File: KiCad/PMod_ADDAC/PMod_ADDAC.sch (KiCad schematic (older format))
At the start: 22 parts, among them J1 Conn_01x12_Male, J2 AudioJack2_SwitchT, U1 TSX632

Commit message: R2R updated
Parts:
- removed C1: 1u, Capacitor_SMD:C_0805_2012Metric_Pad1.15x1.40mm_HandSolder, symbol Device:C_Small
- added C2: 100, Capacitor_SMD:C_0805_2012Metric_Pad1.15x1.40mm_HandSolder, symbol Device:C_Small
- added R18, R19: 1k, Resistor_SMD:R_0805_2012Metric_Pad1.15x1.40mm_HandSolder, symbol Device:R
- R17: value 8k -> 2k
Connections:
- net GND: now also R17.1, U1.5 (+), C2.2
- net VCC: now also C2.1
- net at R1.2, R9.1: now also R19.2
- net at R17.2: now also JP1.1 (A), U1.3 (+), R19.1
- net at JP1.2 (B), U1.1: now also U1.2 (-), R18.1; no longer J2.T, U1.3 (+)
- net at U1.6 (-): now also U1.7
- new net: J2.T, R18.2
- no-connect marks 4 -> 1
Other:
- moved on the sheet: J1, J2, JP1, R1, R10, R11, R12, R13, R14, R15, R16, R2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

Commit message: r2r
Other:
- note added: "3R?\n"
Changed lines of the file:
@@
 Wire Wire Line
 	4550 2100 4550 2150
+Text Notes 5150 3050 0    50   ~ 0
+3R?\n
 $EndSCHEMATC

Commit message: R2RDAC update
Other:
- note added: "add 6.8n tantalum cap?\nboth VCC and VEE"
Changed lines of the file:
@@
 Text Notes 5150 3050 0    50   ~ 0
 3R?\n
+Text Notes 5950 1550 0    50   ~ 0
+add 6.8n tantalum cap?\nboth VCC and VEE
 $EndSCHEMATC

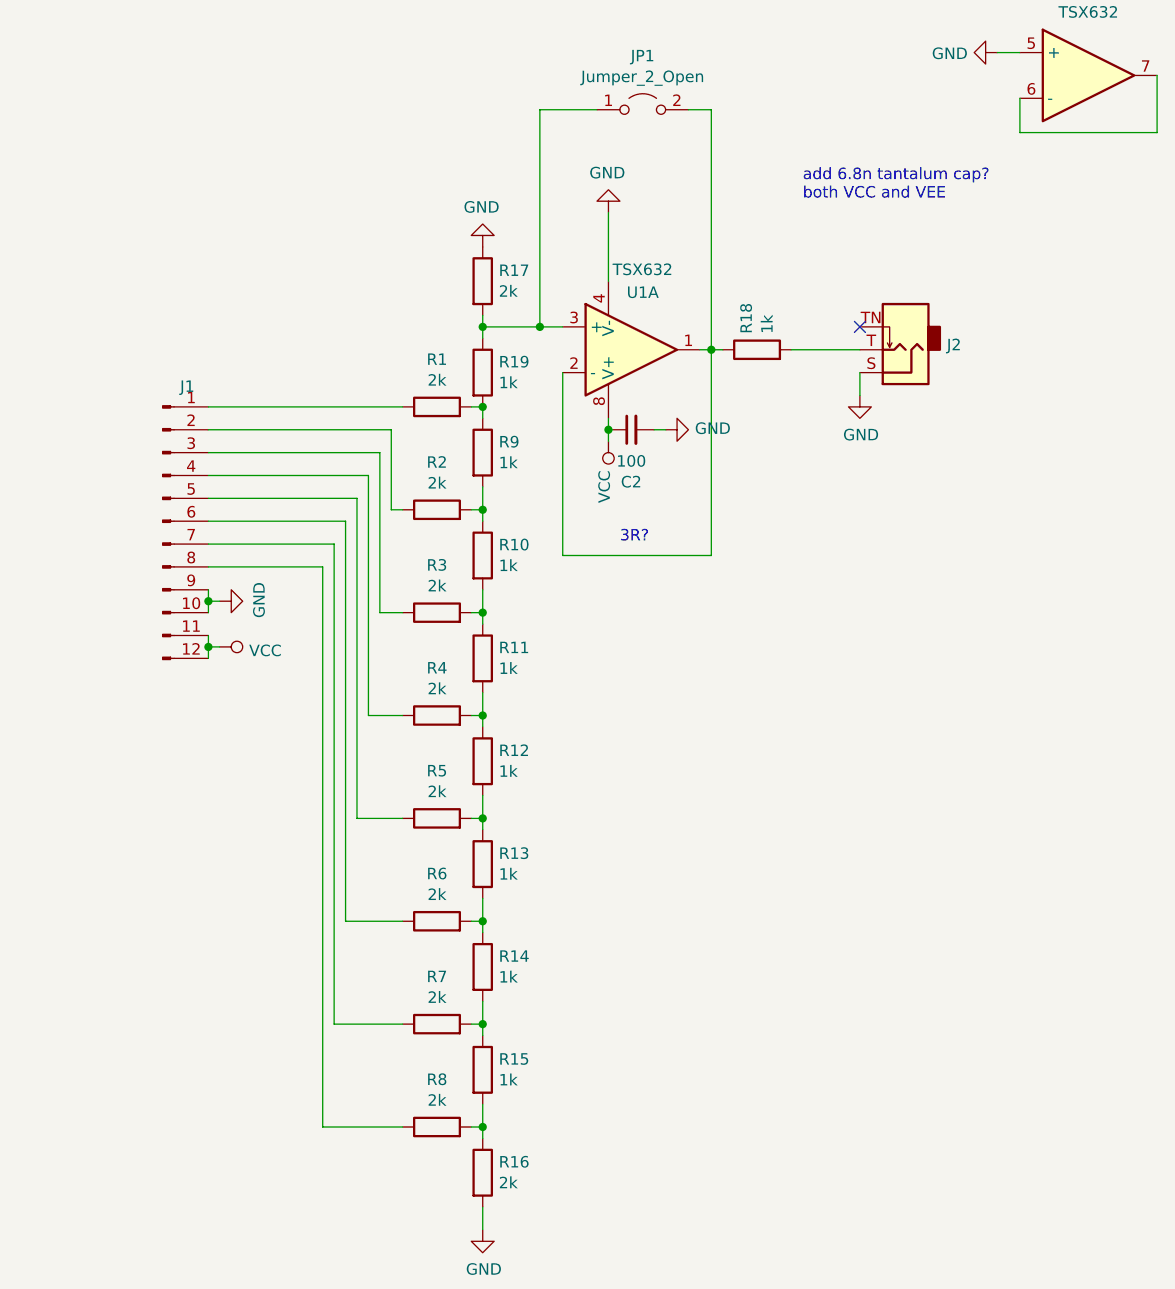
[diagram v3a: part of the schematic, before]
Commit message: fixed R2R orientation
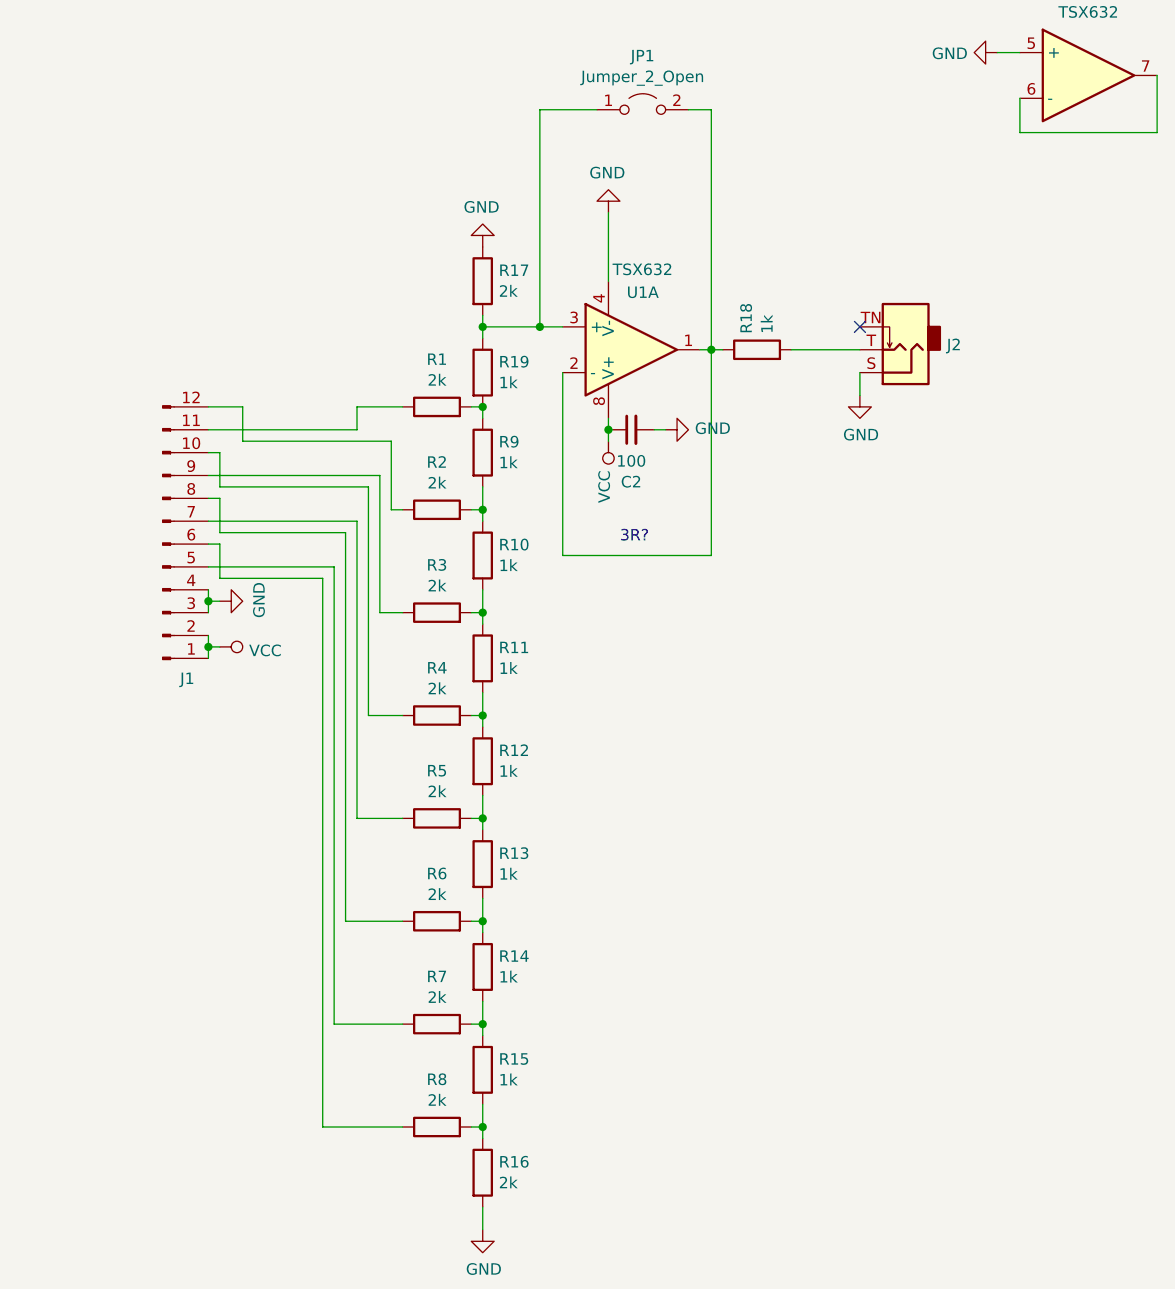
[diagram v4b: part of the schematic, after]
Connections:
- net GND: now also J1.3 (Pin_3), J1.4 (Pin_4); no longer J1.10 (Pin_10), J1.9 (Pin_9)
- net VCC: now also J1.1 (Pin_1), J1.2 (Pin_2); no longer J1.11 (Pin_11), J1.12 (Pin_12)
- net at R1.1: now also J1.11 (Pin_11); no longer J1.1 (Pin_1)
- net at R2.1: now also J1.12 (Pin_12); no longer J1.2 (Pin_2)
- net at R3.1: now also J1.9 (Pin_9); no longer J1.3 (Pin_3)
- net at R4.1: now also J1.10 (Pin_10); no longer J1.4 (Pin_4)
- net at R5.1: now also J1.7 (Pin_7); no longer J1.5 (Pin_5)
- net at R6.1: now also J1.8 (Pin_8); no longer J1.6 (Pin_6)
- net at R7.1: now also J1.5 (Pin_5); no longer J1.7 (Pin_7)
- net at R8.1: now also J1.6 (Pin_6); no longer J1.8 (Pin_8)
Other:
- note removed: "add 6.8n tantalum cap?\nboth VCC and VEE"

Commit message: minor change addac
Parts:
- added C? (x2): 10n, symbol Device:C_Small
- added C?: C_Small, symbol Device:C_Small
- added R? (x5): R, symbol Device:R
- added R? (x2): 1k, symbol Device:R
- added R? (x2): 7k5, symbol Device:R
- added U? (x3): OPAMP, symbol pspice:OPAMP
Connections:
- net GND: now also C?.1, R?.1, R?.2, U?.1 (+), U?.2 (-); no longer U1.5 (+)
- net VCC: now also R?.1
- net at J2.T: now also U1.7, C?.2, R?.1; no longer R18.2
- net at U1.6 (-): now also R?.2, R?.2; no longer U1.7
- new net: C?.2, R?.1, U1.5 (+)
- new net: C?.2, R?.1, R?.1, U?.2 (-)
- new net: R?.2, U?.3
- new net: C?.1, R?.1, R?.2
- new net: C?.1, U?.1 (+), U?.3
- new net: R?.2, U?.1 (+)
- new net: R?.1, R?.2, U?.2 (-)
- new net ADC_A_in: U?.3
- new net ADC_D_out: R?.1
- new net ADC_signal_in: R?.2
- new net DAC_D_out: R18.2, R?.2
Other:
- note added: "Decoupling to hell.........\n"
- note added: "hvis forbindes med eurorack, så brug noise limiting thingies"
- moved on the sheet: C2, J1, J2, JP1, R1, R10, R11, R12, R13, R14, R15, R16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

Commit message: øøøøøøø
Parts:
- added C10, C8, C9: 10n, symbol Device:C_Small
- added C5, C6, C7: 47u, symbol Device:CP_Small
- added FB1, FB2, FB3: Ferrite_Bead_Small, symbol Device:Ferrite_Bead_Small
- added J3: AudioJack2_SwitchT, Audio_conn:Jack_3.5mm_QingPu_WQP-PJ398SM_Vertical_CircularHoles, symbol Connector:AudioJack2_SwitchT
- added J4: Conn_01x16_Male, Connector_PinHeader_2.54mm:PinHeader_2x08_P2.54mm_Vertical, symbol Connector:Conn_01x16_Male
- added R20: 100k, symbol Device:R
- added R21: 10k, symbol Device:R
- added R?: 1k, symbol Device:R
- R27, R28: renamed from R?; value 7k5 -> 820
- gave numbers to parts that had none: 13
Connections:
- net ADC_signal_in: now also R20.1, R21.1
- net GND: now also C10.1, C5.1, C6.2, C7.2, C8.2, C9.1, J3.S, J4.3 (Pin_3), J4.4 (Pin_4), J4.5 (Pin_5), J4.6 (Pin_6), J4.7 (Pin_7), J4.8 (Pin_8), R21.2
- net VCC: no longer R26.1
- net at C4.2, R30.1, U1.7: now also R?.2; no longer J2.T
- new net: J2.T, R?.1
- new net: J3.T, R20.2
- new net: FB1.1, J4.1 (Pin_1), J4.2 (Pin_2)
- new net: FB2.1, J4.10 (Pin_10), J4.9 (Pin_9)
- new net: FB3.1, J4.11 (Pin_11), J4.12 (Pin_12)
- new net: J4.13 (Pin_13), J4.14 (Pin_14)
- new net: J4.15 (Pin_15), J4.16 (Pin_16)
- new net +12V: C6.1, C9.2, FB2.2
- new net +5V: C10.2, C7.1, FB3.2, R26.1
- new net -12V: C5.2, C8.1, FB1.2
- no-connect marks 1 -> 2
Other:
- note added: "- sends out voltage. High input impedance?"
- note added: "-12\nGnd\n+12\n+5\nCV\nGate"
- note added: "-high slew rate comparators\n+-12 eller ?"
- note added: "hvis forbindes med eurorack, så brug noise limiting thingies\n\npower supply\n- use 5V voltage regulator\n- ferrite beads & decoupling caps!"
- note removed: "Decoupling to hell.........\n"
- note removed: "hvis forbindes med eurorack, så brug noise limiting thingies"
- moved on the sheet: C3, C4, J2, R27, R28, R29, R30, U1B

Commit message: mer kicad
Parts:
- removed C1: C_Small, symbol Device:C_Small
- removed C10, C3, C4, C8, C9: 10n, symbol Device:C_Small
- removed C2: 100, Capacitor_SMD:C_0805_2012Metric_Pad1.15x1.40mm_HandSolder, symbol Device:C_Small
- removed C5, C6, C7: 47u, symbol Device:CP_Small
- removed FB1, FB2, FB3: Ferrite_Bead_Small, symbol Device:Ferrite_Bead_Small
- removed J1: Conn_01x12_Male, Connector_PinHeader_2.54mm:PinHeader_2x06_P2.54mm_Horizontal, symbol Connector:Conn_01x12_Male
- removed J2, J3: AudioJack2_SwitchT, Audio_conn:Jack_3.5mm_QingPu_WQP-PJ398SM_Vertical_CircularHoles, symbol Connector:AudioJack2_SwitchT
- removed J4: Conn_01x16_Male, Connector_PinHeader_2.54mm:PinHeader_2x08_P2.54mm_Vertical, symbol Connector:Conn_01x16_Male
- removed JP1: Jumper_2_Open, Jumper:SolderJumper-2_P1.3mm_Open_Pad1.0x1.5mm, symbol Jumper:Jumper_2_Open
- removed R1, R16, R17, R2, R3, R4, R5, R6, R7, R8: 2k, Resistor_SMD:R_0805_2012Metric_Pad1.15x1.40mm_HandSolder, symbol Device:R
- removed R10, R11, R12, R13, R14, R15, R18, R19, R9: 1k, Resistor_SMD:R_0805_2012Metric_Pad1.15x1.40mm_HandSolder, symbol Device:R
- removed R20: 100k, symbol Device:R
- removed R21: 10k, symbol Device:R
- removed R22, R23, R24, R25, R26: R, symbol Device:R
- removed R27, R28: 820, symbol Device:R
- removed R29, R30, R?: 1k, symbol Device:R
- removed U1: TSX632, Package_SO:SOIC-8_3.9x4.9mm_P1.27mm, symbol Device:Opamp_Dual_Generic
- removed U2, U3, U4: OPAMP, symbol pspice:OPAMP
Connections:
- no-connect marks 2 -> 0
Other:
- note added: "TO DO:\n- Pull up/down resistors\n- input/output impedance to board\n- according to manual, the driver to the pins should be able to sink at least 5mA\n-NE5532 as opamp/comparator?"
- note removed: "- R2R ladder\n- AC coupling\n- pmod compabilitet (12 pins, hvoraf 4 er power/gnd)\n- power opamp (maybe OPA358)"
- note removed: "- sends out voltage. High input impedance?"
- note removed: "-12\nGnd\n+12\n+5\nCV\nGate"
- note removed: "-high slew rate comparators\n+-12 eller ?"
- note removed: "3R?\n"

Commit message: kicad update
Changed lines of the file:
@@
 $Descr A4 11693 8268
 encoding utf-8
-Sheet 1 5
+Sheet 1 4
 Title ""
 Date ""
@@
 $EndSheet
 $Sheet
-S 6050 2000 500  150
-U 6242C1FD
-F0 "SDADC" 50
-F1 "SDADC.sch" 50
-$EndSheet
-$Sheet
-S 8000 2150 500  150
+S 7050 2000 500  150
 U 6244F096
 F0 "power" 50
